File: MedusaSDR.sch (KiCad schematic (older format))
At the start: 0 parts

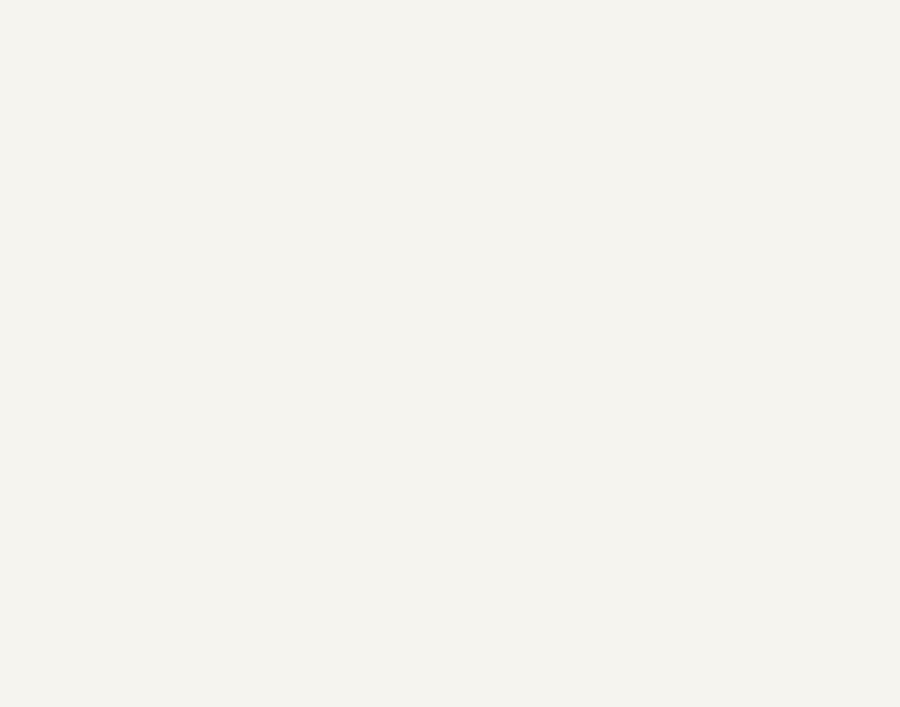
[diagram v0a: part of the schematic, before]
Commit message: add some pmic library
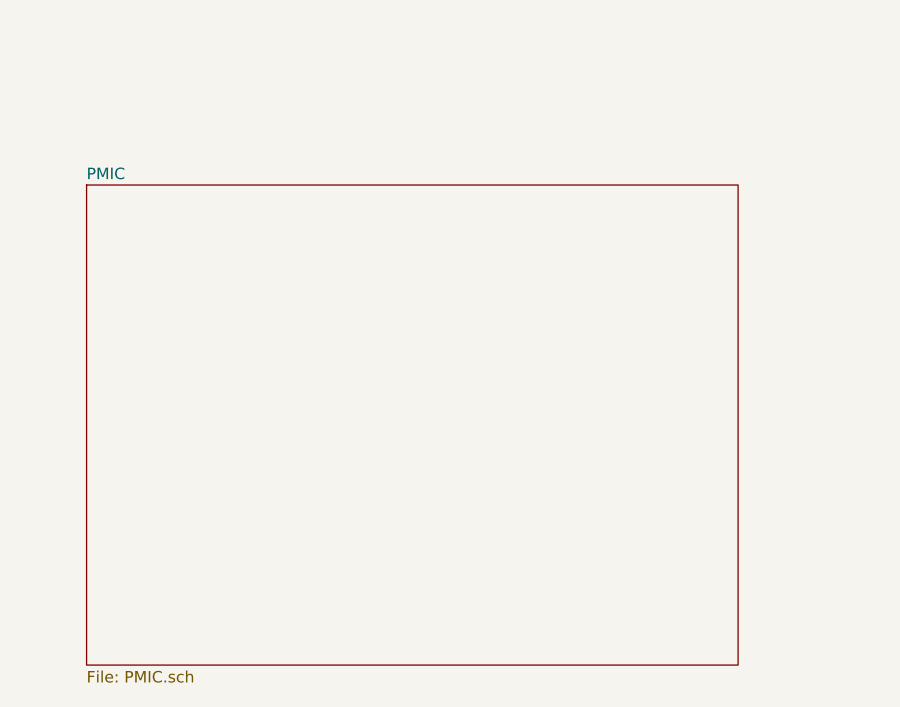
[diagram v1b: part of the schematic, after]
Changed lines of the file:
@@
 EESchema Schematic File Version 4
-LIBS:MedusaSDR-cache
 EELAYER 30 0
 EELAYER END
 $Descr A3 16535 11693
 encoding utf-8
-Sheet 1 11
+Sheet 1 12
 Title ""
 Date ""
@@
 F1 "Transciever.sch" 50
 $EndSheet
+$Sheet
+S 1950 4650 2850 2100
+U 5E0F4BC8
+F0 "PMIC" 50
+F1 "PMIC.sch" 50
+$EndSheet
 $EndSCHEMATC
